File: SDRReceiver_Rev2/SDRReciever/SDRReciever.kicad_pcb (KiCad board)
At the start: 2 copper layers, 100 x 100 mm, 78 parts, among them J1 Conn_Coaxial, J10 I_0, J11 I_180, J12 Q_90, J13 Q_270, J14 I_OUT, J15 Q_OUT, J16 5V, J17 4.3V, J18 Conn_01x02_Female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

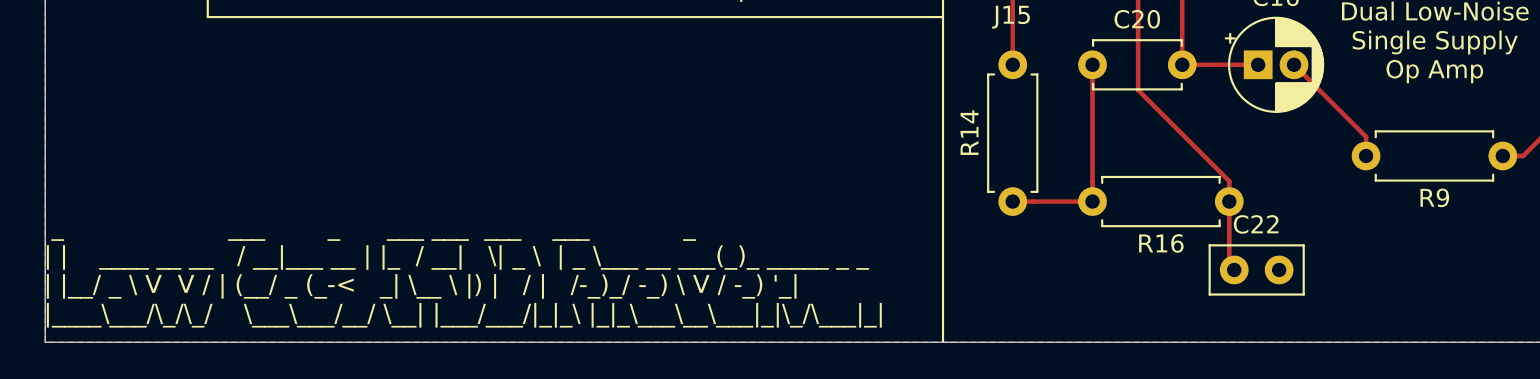
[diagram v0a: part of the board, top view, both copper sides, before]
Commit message: Fixed the Rev2 schematic from being pulled apart for screenshots
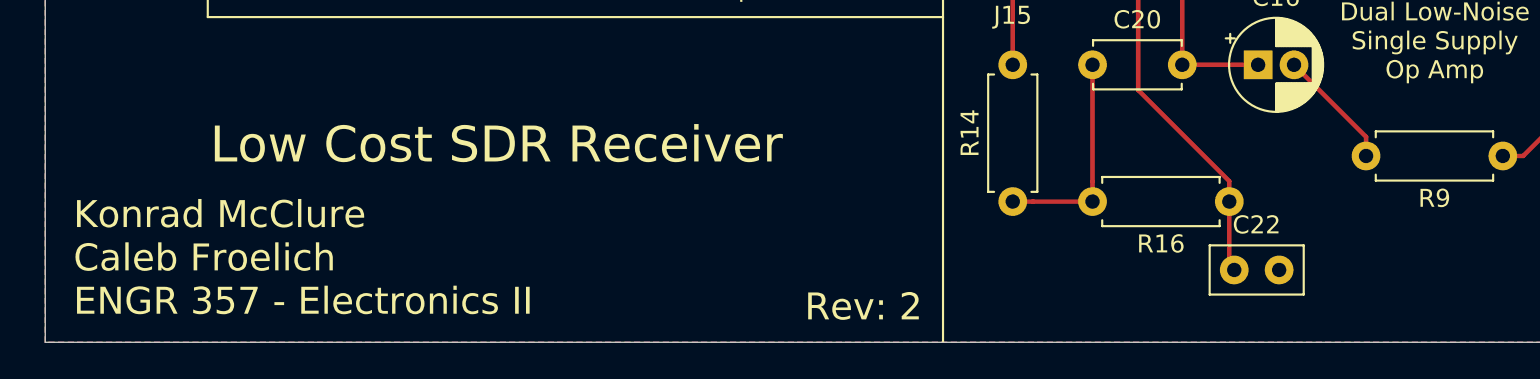
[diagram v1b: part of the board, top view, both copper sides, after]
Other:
- board text added: "Konrad McClure Caleb Froelich ENGR 357 - Electronics II"
- board text added: "Low Cost SDR Receiver"
- board text added: "Rev: 2"
- board text removed: "_ ___ _ ___ ___ ___ ___ _ | | ____ __ __ / __|___ __ | |_ / __| \| _ \ | _ \___ __ ___(_)_ _____ _ _ | |__/ _ \ V V / | (__/ _ (_-< _| \__ \ |) | / | /-_)_/ -_) \ V / -_) '_| |____\___/\_/\_/ \___\___/__/ \__| |___/___/|_|_\ |_|_\___\__\___|_|\_/\___|_|"
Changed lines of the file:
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@@
   (general
     (thickness 1.6)
-    (drawings 76)
+    (drawings 78)
     (tracks 386)
     (zones 0)
@@
   (page A4)
   (layers
-    (0 F.Cu signal hide)
-    (31 B.Cu signal hide)
+    (0 F.Cu signal)
+    (31 B.Cu signal)
     (32 B.Adhes user)
     (33 F.Adhes user)
@@
     (44 Edge.Cuts user)
     (45 Margin user)
-    (46 B.CrtYd user)
-    (47 F.CrtYd user)
+    (46 B.CrtYd user hide)
+    (47 F.CrtYd user hide)
     (48 B.Fab user)
-    (49 F.Fab user)
+    (49 F.Fab user hide)
   )
   (setup
@@
       (padsonsilk false)
       (subtractmaskfromsilk false)
-      (outputformat 1)
+      (outputformat 4)
       (mirror false)
-      (drillshape 1)
+      (drillshape 0)
       (scaleselection 1)
-      (outputdirectory ""))
+      (outputdirectory "../documents/"))
   )
   (net 0 "")
@@
     )
   )
-  (gr_text "  _                     ___        _      ___ ___  ___    ___            _             \n | |    ____ __ __   / __|___ __ | |_  / __|   \\| _ \\  | _ \\___ __ ___(_)_ _____ _ _ \n | |__/ _ \\ V  V / | (__/ _ (_-<   _| \\__ \\ |) |   / |   /-_)_/ -_) \\ V / -_) '_|\n |____\\___/\\_/\\_/    \\___\\___/__/ \\__| |___/___/|_|_\\ |_|_\\___\\__\\___|_|\\_/\\___|_| " (at 74.48 140.98) (layer F.SilkS)
-    (effects (font (size 1 1) (thickness 0.15)) (justify left))
+  (gr_text "Rev: 2" (at 120.59 143.03) (layer F.SilkS)
+    (effects (font (size 1.5 1.5) (thickness 0.2)))
+  )
+  (gr_text "Low Cost SDR Receiver" (at 100.14 134) (layer F.SilkS)
+    (effects (font (size 2 2) (thickness 0.3)))
+  )
+  (gr_text "Konrad McClure\nCaleb Froelich\nENGR 357 - Electronics II" (at 76.57 140.3) (layer F.SilkS)
+    (effects (font (size 1.5 1.5) (thickness 0.2)) (justify left))
   )
   (gr_line (start 103.474 112.252) (end 104.006 112.784) (layer F.SilkS) (width 0.12))
@@
   (segment (start 171.18 119.093502) (end 171.18 123.55) (width 0.25) (layer F.Cu) (net 45))
   (segment (start 171.18 117.75) (end 171.18 119.093502) (width 0.25) (layer F.Cu) (net 45))
-  (segment (start 113.772 112.678) (end 113.772 115.918) (width 0.25) (layer F.Cu) (net 70))
-  (segment (start 117.582 108.868) (end 113.772 112.678) (width 0.25) (layer F.Cu) (net 70))
-  (segment (start 112.502 111.408) (end 112.502 115.918) (width 0.25) (layer F.Cu) (net 71))
-  (segment (start 109.962 108.868) (end 112.502 111.408) (width 0.25) (layer F.Cu) (net 71))
-  (segment (start 94.087 111.789) (end 94.087 115.283) (width 0.25) (layer F.Cu) (net 72))
-  (segment (start 90.658 108.36) (end 94.087 111.789) (width 0.25) (layer F.Cu) (net 72))
-  (segment (start 95.357 111.281) (end 95.357 115.283) (width 0.25) (layer F.Cu) (net 73))
-  (segment (start 98.278 108.36) (end 95.357 111.281) (width 0.25) (layer F.Cu) (net 73))
   (segment (start 89.834846 86.141) (end 90.787 86.141) (width 1.06372) (layer F.Cu) (net 46))
   (segment (start 88.564846 84.871) (end 89.834846 86.141) (width 1.06372) (layer F.Cu) (net 46))
@@
   (segment (start 132.715 72.485) (end 133.255 73.025) (width 1.06372) (layer F.Cu) (net 69))
   (segment (start 132.715 67.945) (end 132.715 72.485) (width 1.06372) (layer F.Cu) (net 69))
+  (segment (start 113.772 112.678) (end 113.772 115.918) (width 0.25) (layer F.Cu) (net 70))
+  (segment (start 117.582 108.868) (end 113.772 112.678) (width 0.25) (layer F.Cu) (net 70))
   (segment (start 112.456 113.994) (end 117.582 108.868) (width 0.25) (layer B.Cu) (net 70))
   (segment (start 106.666 113.994) (end 112.456 113.994) (width 0.25) (layer B.Cu) (net 70))
+  (segment (start 112.502 111.408) (end 112.502 115.918) (width 0.25) (layer F.Cu) (net 71))
+  (segment (start 109.962 108.868) (end 112.502 111.408) (width 0.25) (layer F.Cu) (net 71))
   (segment (start 108.152 108.868) (end 108.83063 108.868) (width 0.25) (layer B.Cu) (net 71))
   (segment (start 108.83063 108.868) (end 109.962 108.868) (width 0.25) (layer B.Cu) (net 71))
   (segment (start 106.666 110.354) (end 108.152 108.868) (width 0.25) (layer B.Cu) (net 71))
   (segment (start 106.666 111.454) (end 106.666 110.354) (width 0.25) (layer B.Cu) (net 71))
+  (segment (start 94.087 111.789) (end 94.087 115.283) (width 0.25) (layer F.Cu) (net 72))
+  (segment (start 90.658 108.36) (end 94.087 111.789) (width 0.25) (layer F.Cu) (net 72))
   (segment (start 96.146 113.848) (end 90.658 108.36) (width 0.25) (layer B.Cu) (net 72))
   (segment (start 101.612 113.848) (end 96.146 113.848) (width 0.25) (layer B.Cu) (net 72))
+  (segment (start 95.357 111.281) (end 95.357 115.283) (width 0.25) (layer F.Cu) (net 73))
+  (segment (start 98.278 108.36) (end 95.357 111.281) (width 0.25) (layer F.Cu) (net 73))
   (segment (start 98.664 108.36) (end 98.278 108.36) (width 0.25) (layer B.Cu) (net 73))
   (segment (start 101.612 111.308) (end 98.664 108.36) (width 0.25) (layer B.Cu) (net 73))
@@
       )
     )
+  )
+  (zone (net 0) (net_name "") (layers F&B.Cu) (hatch edge 0.508)
+    (connect_pads (clearance 0.508))
+    (min_thickness 0.254)
+    (keepout (tracks not_allowed) (vias not_allowed) (copperpour not_allowed))
+    (fill (arc_segments 32) (thermal_gap 0.508) (thermal_bridge_width 0.508))
+    (polygon
+      (pts
+        (xy 80.48 64.53) (xy 75.01 64.53) (xy 75.01 62.84) (xy 80.48 62.84)
+      )
+    )
+  )
+  (zone (net 0) (net_name "") (layers F&B.Cu) (hatch edge 0.508)
+    (connect_pads (clearance 0.508))
+    (min_thickness 0.254)
+    (keepout (tracks not_allowed) (vias not_allowed) (copperpour not_allowed))
+    (fill (arc_segments 32) (thermal_gap 0.508) (thermal_bridge_width 0.508))
+    (polygon
+      (pts
+        (xy 80.45 68.73) (xy 75.01 68.73) (xy 75.01 67.11) (xy 80.45 67.11)
+      )
+    )
